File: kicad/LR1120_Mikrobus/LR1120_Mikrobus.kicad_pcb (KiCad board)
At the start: 2 copper layers, 5 parts

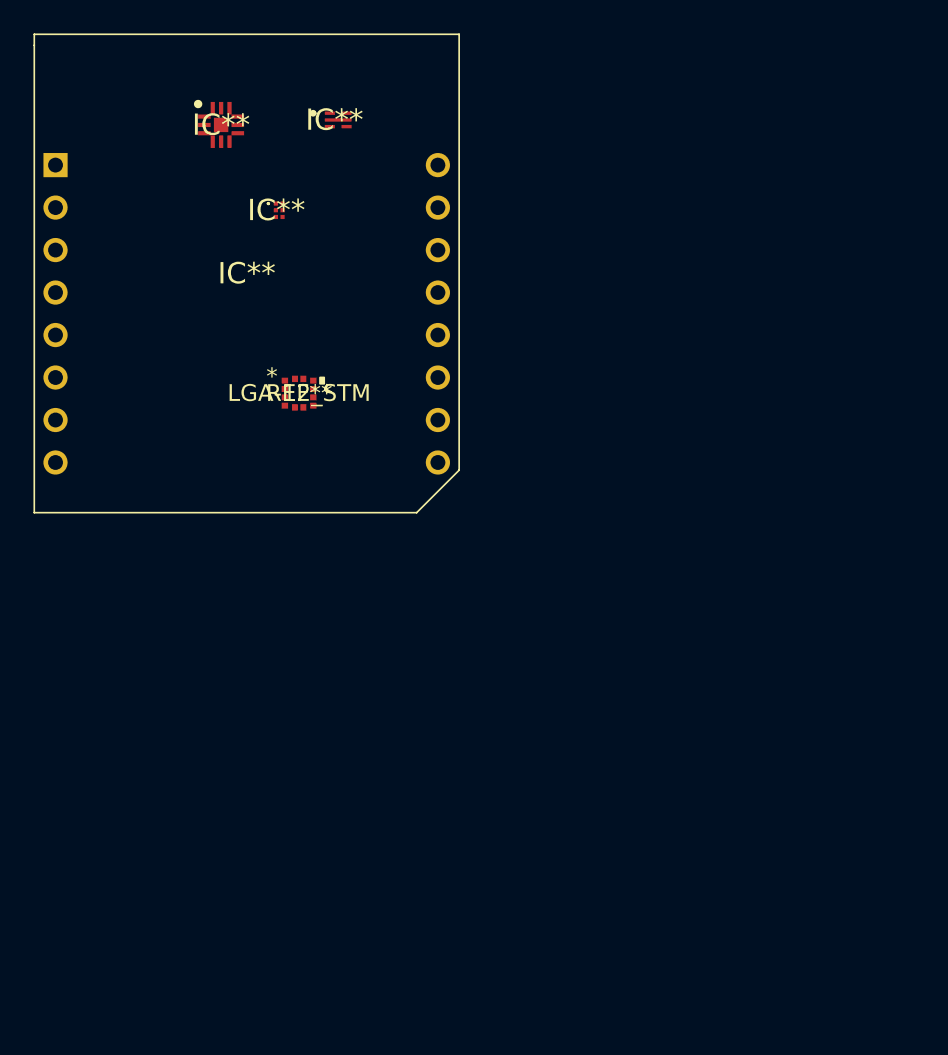
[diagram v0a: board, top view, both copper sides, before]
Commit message: created board edges, added ant
Created board edges, placed antennas
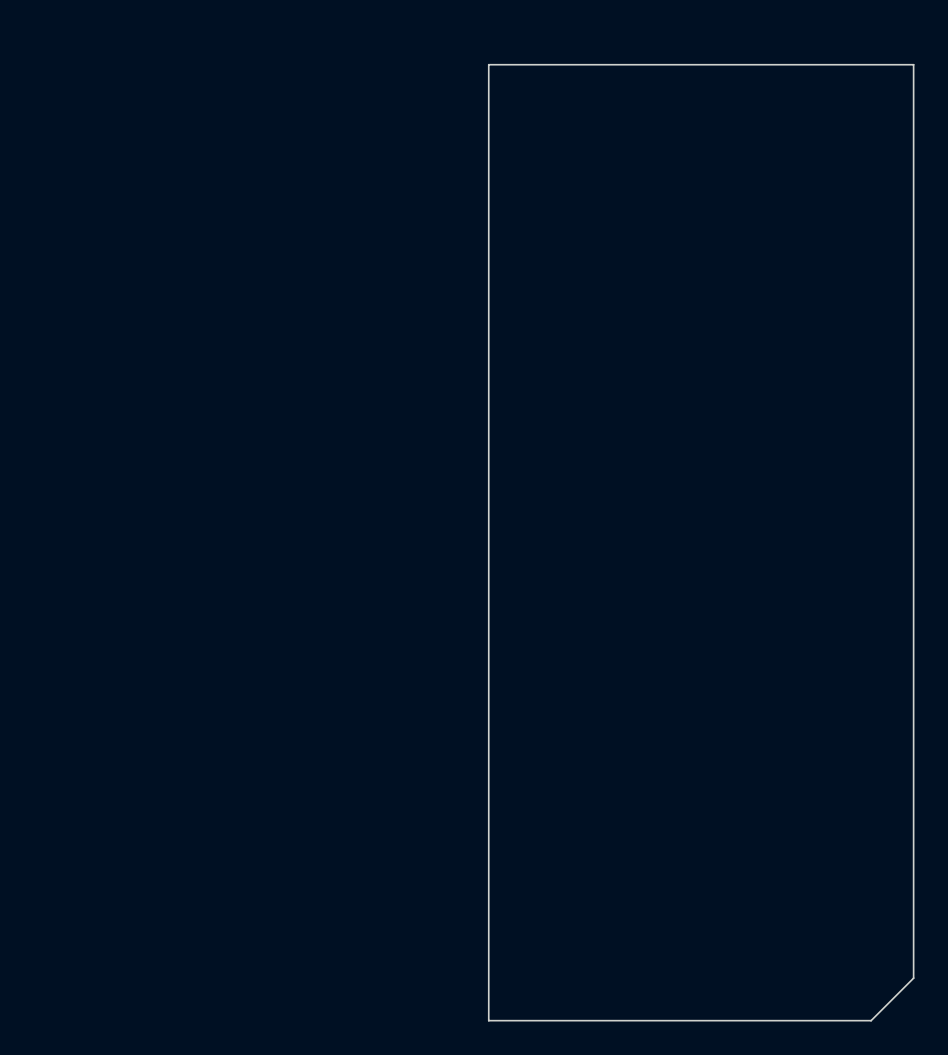
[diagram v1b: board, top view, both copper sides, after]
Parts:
- removed IC**: QFN50P200X200X65-13N-D, SKY13588:QFN50P200X200X65-13N-D
- removed IC**: M24128BFMH6TG, M24128B:M24128BFMH6TG
- removed IC**: BGS12SN6E6327XTSA1, BGA524N6:BGS12SN6E6327XTSA1
- removed IC**: MIKROE924, KiCad:MIKROE924
- removed REF**: LGA-12_STM, LIS2DE12:LIS2DE12TR
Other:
- board outline added: 25.4 x 57.2 mm

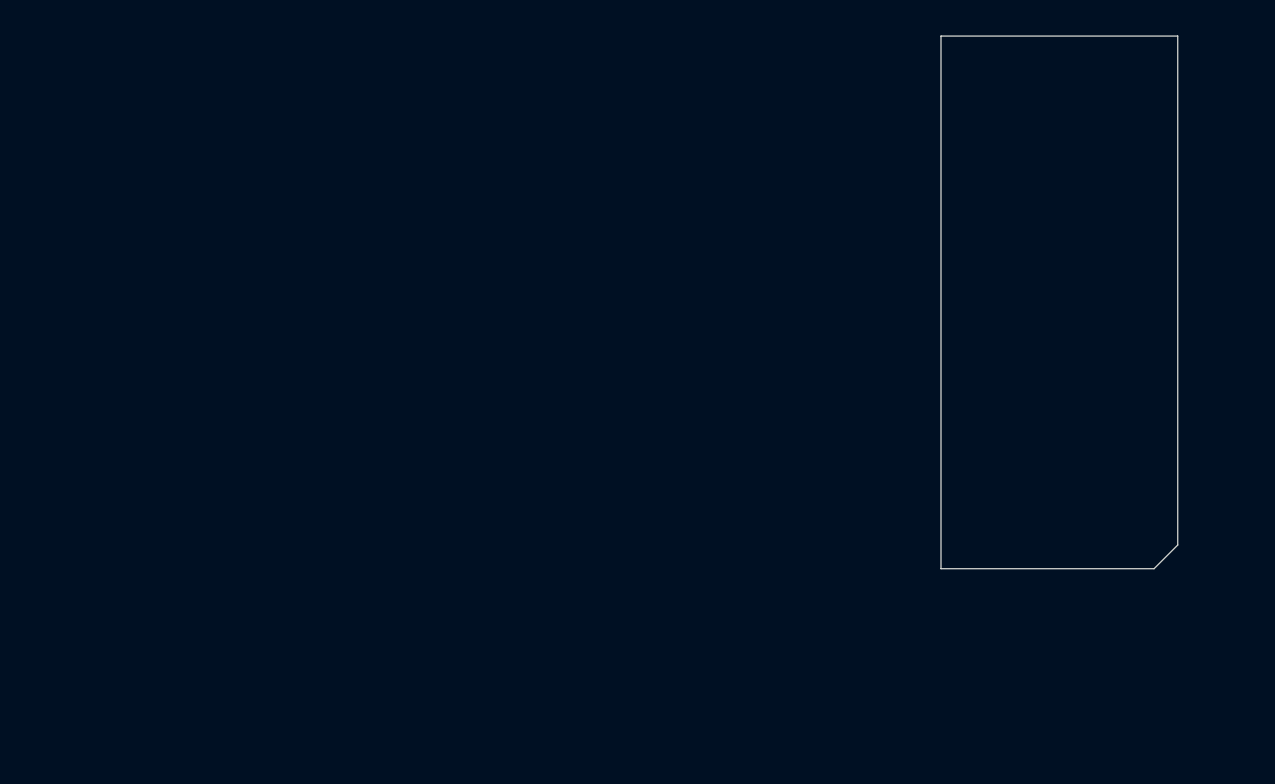
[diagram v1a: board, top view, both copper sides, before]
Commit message: PCB:populated comp placed connectors
Populated the PCB with all the components. Placed and locked the connectors
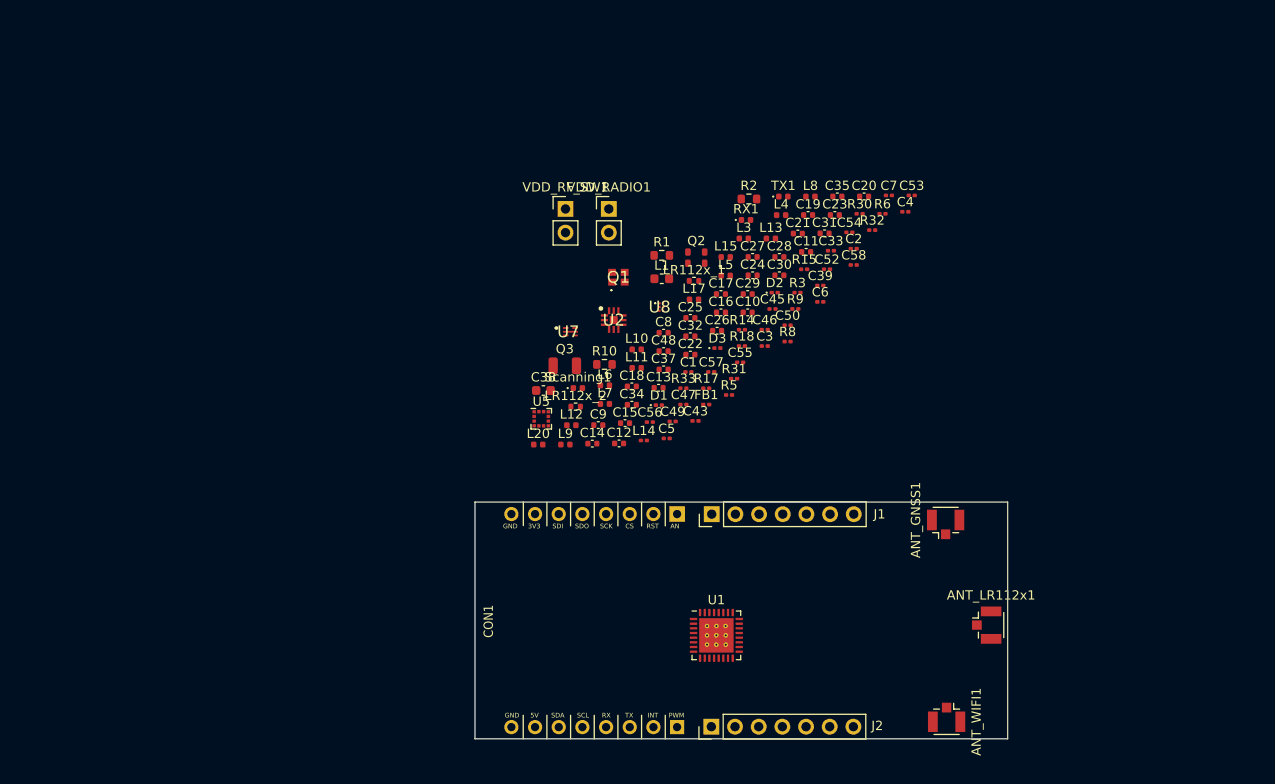
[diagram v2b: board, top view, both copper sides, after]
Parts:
- added ANT_GNSS1: Conn_Coaxial, Connector_Coaxial:U.FL_Hirose_U.FL-R-SMT-1_Vertical, F.Cu at (150.5, 102.4)
- added ANT_LR112x1: Conn_Coaxial, Connector_Coaxial:U.FL_Hirose_U.FL-R-SMT-1_Vertical, F.Cu at (154.9, 113.2)
- added ANT_WIFI1: Conn_Coaxial, Connector_Coaxial:U.FL_Hirose_U.FL-R-SMT-1_Vertical, F.Cu at (150.6, 123.1)
- added C1: 100nF, Capacitor_SMD:C_0201_0603Metric, F.Cu at (122.9, 86.0)
- added C10: 12pF, Capacitor_SMD:C_0402_1005Metric, F.Cu at (129.3, 79.7)
- added C11: NC, Capacitor_SMD:C_0402_1005Metric, F.Cu at (135.5, 73.2)
- added C12: 0.5pF, Capacitor_SMD:C_0402_1005Metric, F.Cu at (115.5, 93.7)
- added C13: NC, Capacitor_SMD:C_0402_1005Metric, F.Cu at (119.7, 87.7)
- added C14: 6.8pF, Capacitor_SMD:C_0402_1005Metric, F.Cu at (112.6, 93.7)
- added C15: 12pF, Capacitor_SMD:C_0402_1005Metric, F.Cu at (116.1, 91.5)
- added C16: NC, Capacitor_SMD:C_0402_1005Metric, F.Cu at (126.4, 79.7)
- added C17: 0.5pF, Capacitor_SMD:C_0402_1005Metric, F.Cu at (126.4, 77.7)
- added C18: 1pF, Capacitor_SMD:C_0402_1005Metric, F.Cu at (116.8, 87.6)
- added C19: 1.5pF, Capacitor_SMD:C_0402_1005Metric, F.Cu at (135.7, 69.2)
- added C2: 47pF, Capacitor_SMD:C_0201_0603Metric, F.Cu at (140.6, 72.8)
- added C20: NC, Capacitor_SMD:C_0402_1005Metric, F.Cu at (141.8, 67.2)
- added C21: 12pF, Capacitor_SMD:C_0402_1005Metric, F.Cu at (134.6, 71.2)
- added C22: 1pF, Capacitor_SMD:C_0402_1005Metric, F.Cu at (123.1, 84.2)
- added C23: 1.5pF, Capacitor_SMD:C_0402_1005Metric, F.Cu at (138.6, 69.2)
- added C24: 0.5pF, Capacitor_SMD:C_0402_1005Metric, F.Cu at (129.8, 75.7)
- added C25: 12pF, Capacitor_SMD:C_0402_1005Metric, F.Cu at (123.1, 80.2)
- added C26: 0.5pF, Capacitor_SMD:C_0402_1005Metric, F.Cu at (126.0, 81.6)
- added C27: 1.3pF, Capacitor_SMD:C_0402_1005Metric, F.Cu at (129.8, 73.7)
- added C28: 1.6pF, Capacitor_SMD:C_0402_1005Metric, F.Cu at (132.7, 73.7)
- added C29: 33pF, Capacitor_SMD:C_0402_1005Metric, F.Cu at (129.3, 77.7)
- added C3: 470nF, Capacitor_SMD:C_0201_0603Metric, F.Cu at (131.1, 83.3)
- added C30: 0.7pF, Capacitor_SMD:C_0402_1005Metric, F.Cu at (132.7, 75.7)
- added C31: 0.5pF, Capacitor_SMD:C_0402_1005Metric, F.Cu at (137.5, 71.2)
- added C32: 0.5pF, Capacitor_SMD:C_0402_1005Metric, F.Cu at (123.1, 82.2)
- added C33: 12pF, Capacitor_SMD:C_0201_0603Metric, F.Cu at (138.2, 73.0)
- added C34: 12pF, Capacitor_SMD:C_0402_1005Metric, F.Cu at (116.8, 89.6)
- added C35: 12pF, Capacitor_SMD:C_0402_1005Metric, F.Cu at (138.9, 67.2)
- added C37: 12pF, Capacitor_SMD:C_0402_1005Metric, F.Cu at (120.2, 85.8)
- added C38: 12pF, Capacitor_SMD:C_0603_1608Metric, F.Cu at (107.3, 88.0)
- added C39: 1.5pF, Capacitor_SMD:C_0201_0603Metric, F.Cu at (137.1, 76.8)
- added C4: 100nF, Capacitor_SMD:C_0201_0603Metric, F.Cu at (146.2, 68.8)
- added C43: 1nF, Capacitor_SMD:C_0201_0603Metric, F.Cu at (123.7, 91.3)
- added C45: 1nF, Capacitor_SMD:C_0201_0603Metric, F.Cu at (131.9, 79.3)
- added C46: 1nF, Capacitor_SMD:C_0201_0603Metric, F.Cu at (131.1, 81.5)
- added C47: 1pF, Capacitor_SMD:C_0201_0603Metric, F.Cu at (122.4, 89.5)
- added C48: 1pF, Capacitor_SMD:C_0402_1005Metric, F.Cu at (120.2, 83.8)
- added C49: 0.5pF, Capacitor_SMD:C_0201_0603Metric, F.Cu at (121.2, 91.3)
- added C5: 2.2nF, Capacitor_SMD:C_0201_0603Metric, F.Cu at (120.6, 93.2)
- added C50: 1pF, Capacitor_SMD:C_0201_0603Metric, F.Cu at (133.5, 81.0)
- added C52: NC, Capacitor_SMD:C_0201_0603Metric, F.Cu at (137.8, 75.0)
- added C53: NC, Capacitor_SMD:C_0201_0603Metric, F.Cu at (146.9, 67.1)
- added C54: 33pF, Capacitor_SMD:C_0201_0603Metric, F.Cu at (140.2, 71.1)
- added C55: 0.5pF, Capacitor_SMD:C_0201_0603Metric, F.Cu at (128.4, 85.0)
- added C56: 0.5pF, Capacitor_SMD:C_0201_0603Metric, F.Cu at (118.8, 91.4)
- added C57: 1.8pF, Capacitor_SMD:C_0201_0603Metric, F.Cu at (125.3, 86.0)
- added C58: 1nF, Capacitor_SMD:C_0201_0603Metric, F.Cu at (140.6, 74.6)
- added C6: 47pF, Capacitor_SMD:C_0201_0603Metric, F.Cu at (137.1, 78.5)
- added C7: 47pF, Capacitor_SMD:C_0201_0603Metric, F.Cu at (144.4, 67.1)
- added C8: NC, Capacitor_SMD:C_0402_1005Metric, F.Cu at (120.2, 81.8)
- added C9: 0.5pF, Capacitor_SMD:C_0402_1005Metric, F.Cu at (113.2, 91.7)
- added CON1: MIKROBUS_MODULE_CONN, Mikrobus:MIKROBUS_MODULE_CONN, F.Cu at (121.7, 101.3)
- added D1: RClamp2451ZA, Diode_SMD:D_0201_0603Metric, F.Cu at (119.7, 89.6)
- added D2: RClamp2451ZA, Diode_SMD:D_0201_0603Metric, F.Cu at (132.2, 77.5)
- added D3: RClamp2451ZA, Diode_SMD:D_0201_0603Metric, F.Cu at (126.0, 83.5)
- added FB1: FerriteBead, Inductor_SMD:L_0201_0603Metric, F.Cu at (124.8, 89.5)
- added J1: Conn_01x07, Connector_PinHeader_2.54mm:PinHeader_1x07_P2.54mm_Vertical, F.Cu at (125.4, 101.3)
- added J2: Conn_01x07, Connector_PinHeader_2.54mm:PinHeader_1x07_P2.54mm_Vertical, F.Cu at (125.4, 124.1)
- added L1: 10uH, Inductor_SMD:L_0603_1608Metric, F.Cu at (120.0, 76.0)
- added L10: 33nH, Inductor_SMD:L_0402_1005Metric, F.Cu at (117.3, 83.6)
- added L11: 9.5nH, Inductor_SMD:L_0402_1005Metric, F.Cu at (117.3, 85.6)
- added L12: 33nH, Inductor_SMD:L_0402_1005Metric, F.Cu at (110.3, 91.8)
- added L13: 9.5nH, Inductor_SMD:L_0402_1005Metric, F.Cu at (131.8, 71.7)
- added L14: 33nH, Inductor_SMD:L_0201_0603Metric, F.Cu at (118.1, 93.4)
- added L15: 3.6nH, Inductor_SMD:L_0402_1005Metric, F.Cu at (126.9, 73.7)
- added L17: 9.5nH, Inductor_SMD:L_0402_1005Metric, F.Cu at (123.5, 78.3)
- added L20: 3.6nH, Inductor_SMD:L_0402_1005Metric, F.Cu at (106.8, 93.8)
- added L3: 9.5nH, Inductor_SMD:L_0402_1005Metric, F.Cu at (128.8, 71.7)
- added L4: 9.5nH, Inductor_SMD:L_0402_1005Metric, F.Cu at (132.8, 69.2)
- added L5: 9.5nH, Inductor_SMD:L_0402_1005Metric, F.Cu at (126.9, 75.7)
- added L6: 9.5nH, Inductor_SMD:L_0402_1005Metric, F.Cu at (113.9, 87.5)
- added L7: 9.5nH, Inductor_SMD:L_0402_1005Metric, F.Cu at (113.9, 89.5)
- added L8: 9.5nH, Inductor_SMD:L_0402_1005Metric, F.Cu at (136.0, 67.2)
- added L9: 9.5nH, Inductor_SMD:L_0402_1005Metric, F.Cu at (109.7, 93.8)
- added LR112x_1: 0R, Resistor_SMD:R_0402_1005Metric, F.Cu at (123.5, 76.3)
- added LR112x_2: 0R, Resistor_SMD:R_0402_1005Metric, F.Cu at (110.8, 89.8)
- added Q1: NX2016SA-32M-EXS00A-CS06465, EXS00A-CS06465:NX2016SA32MEXS00ACS06465, F.Cu at (115.4, 75.9)
- added Q2: NT2016SA-32M-END4263A, TXCO:NT2016SA-32M-END4263A, F.Cu at (123.7, 73.8)
- added Q3: NX3215SA, TXCO:NX3215SA, F.Cu at (109.6, 85.4)
- added R1: NC, Resistor_SMD:R_0603_1608Metric, F.Cu at (120.0, 73.5)
- added R10: NC, Resistor_SMD:R_0603_1608Metric, F.Cu at (113.9, 85.2)
- added R14: 330, Resistor_SMD:R_0201_0603Metric, F.Cu at (128.6, 81.5)
- added R15: 330, Resistor_SMD:R_0201_0603Metric, F.Cu at (135.3, 75.0)
- added R17: NC, Resistor_SMD:R_0201_0603Metric, F.Cu at (124.8, 87.8)
- added R18: 0R, Resistor_SMD:R_0201_0603Metric, F.Cu at (128.6, 83.3)
- added R2: 0R, Resistor_SMD:R_0603_1608Metric, F.Cu at (129.4, 67.5)
- added R3: 220, Resistor_SMD:R_0201_0603Metric, F.Cu at (134.6, 77.5)
- added R30: 330, Resistor_SMD:R_0201_0603Metric, F.Cu at (141.3, 69.1)
- added R31: NC, Resistor_SMD:R_0201_0603Metric, F.Cu at (127.8, 86.8)
- added R32: NC, Resistor_SMD:R_0201_0603Metric, F.Cu at (142.6, 70.8)
- added R33: R, Resistor_SMD:R_0201_0603Metric, F.Cu at (122.4, 87.8)
- added R5: NC, Resistor_SMD:R_0201_0603Metric, F.Cu at (127.3, 88.5)
- added R6: NC, Resistor_SMD:R_0201_0603Metric, F.Cu at (143.7, 69.1)
- added R8: 0R, Resistor_SMD:R_0201_0603Metric, F.Cu at (133.5, 82.8)
- added R9: 100, Resistor_SMD:R_0201_0603Metric, F.Cu at (134.4, 79.3)
- added RX1: LED, LED_SMD:LED_0402_1005Metric, F.Cu at (129.1, 69.7)
- added Scanning1: LED, LED_SMD:LED_0402_1005Metric, F.Cu at (111.0, 87.8)
- added TX1: LED, LED_SMD:LED_0402_1005Metric, F.Cu at (133.1, 67.2)
- added U1: LR1120, Package_DFN_QFN:QFN-32-1EP_5x5mm_P0.5mm_EP3.7x3.7mm_ThermalVias, F.Cu at (125.9, 114.3)
- added U2: SKY13588-460LF, SKY13588:QFN50P200X200X65-13N-D, F.Cu at (114.9, 80.5)
- added U5: LIS2DE12, Package_LGA:LGA-12_2x2mm_P0.5mm, F.Cu at (107.1, 91.1)
- added U7: M24128-BFMH6TG, M24128B:M24128BFMH6TG, F.Cu at (110.2, 81.7)
- added U8: BGA524N6E6327XTSA1, BGA524N6:BGS12SN6E6327XTSA1, F.Cu at (119.8, 79.1)
- added VDD_RADIO1: Jumper_2_Bridged, Connector_PinHeader_2.54mm:PinHeader_1x02_P2.54mm_Vertical, F.Cu at (114.4, 68.5)
- added VDD_RF_SW1: Jumper_2_Bridged, Connector_PinHeader_2.54mm:PinHeader_1x02_P2.54mm_Vertical, F.Cu at (109.7, 68.5)
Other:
- board size 25.4 x 57.2 mm -> 57.2 x 25.4 mm
- copper layers 2 -> 4

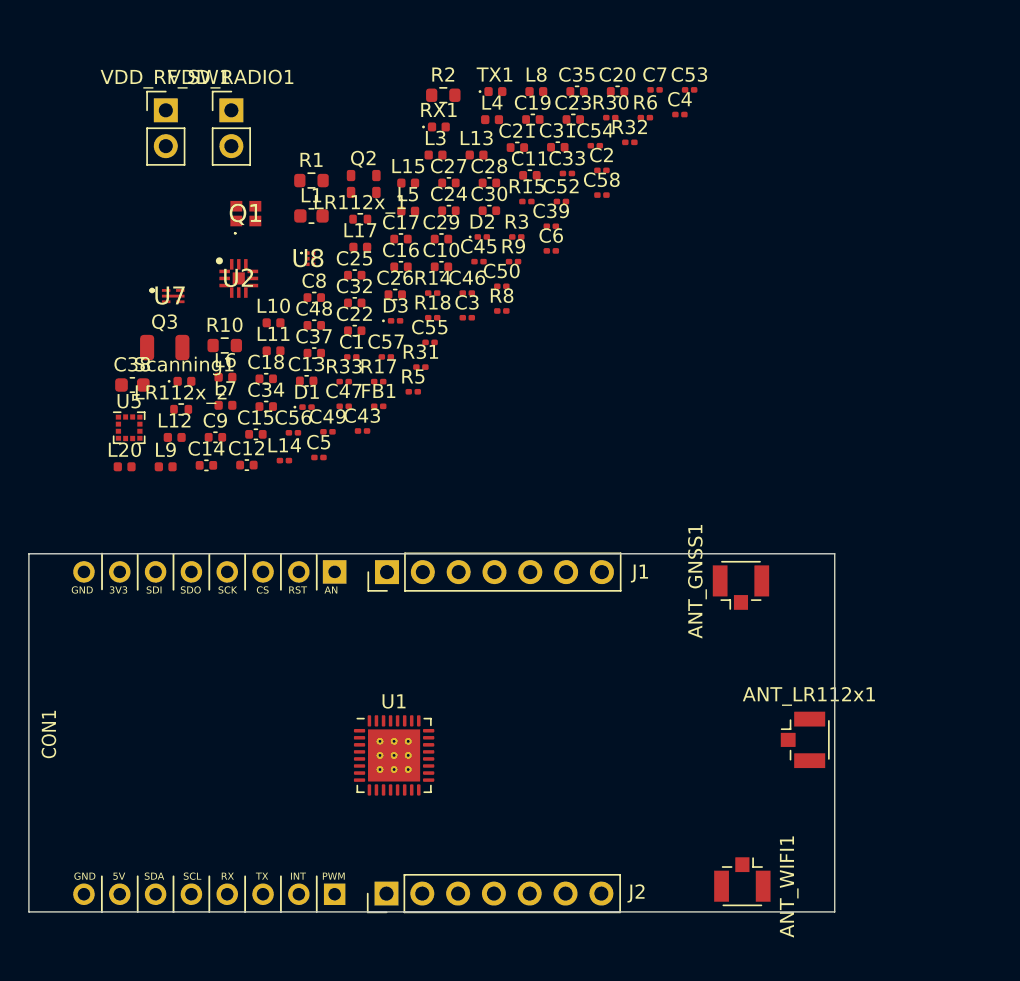
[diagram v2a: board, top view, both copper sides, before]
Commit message: other components placed
placed: U2, U8, U1. Q1, Q2 Q3.
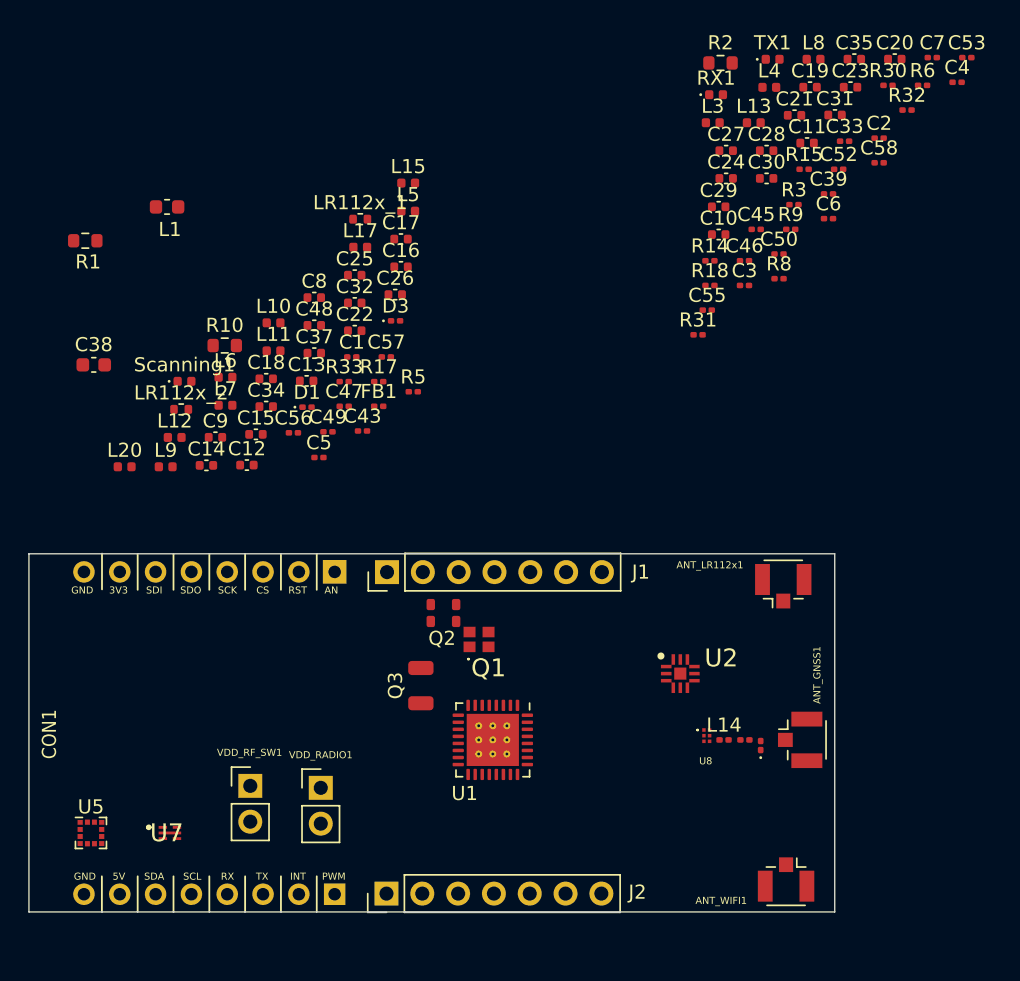
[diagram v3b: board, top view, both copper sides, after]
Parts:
- moved VDD_RADIO1 48.5 mm to (120.7, 116.6)
- moved VDD_RF_SW1 48.3 mm to (115.7, 116.5)
- moved U8 44.0 mm to (147.9, 112.9)
- moved C54 43.5 mm to (150.8, 113.2), turned to 180 degrees
- moved U2 42.0 mm to (146.2, 108.5)
- moved D2 41.1 mm to (151.9, 113.6), turned to 90 degrees
- moved U7 38.1 mm to (110.0, 119.8)
- moved L14 36.9 mm to (149.3, 113.2)
- moved Q1 34.4 mm to (131.9, 106.1)
- moved Q2 30.9 mm to (129.4, 104.2)
- moved Q3 30.1 mm to (127.8, 109.3), turned to 90 degrees
- moved U5 28.9 mm to (104.4, 119.8)
- moved C2 19.8 mm to (160.3, 70.5)
- moved C21 19.8 mm to (154.3, 68.9)
- moved C4 19.8 mm to (165.8, 66.6)
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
